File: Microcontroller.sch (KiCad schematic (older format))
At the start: 19 parts, among them P2 UART, P3 USB_B, P5 JTAG, U5 ATMEGA32U4RC-A, Y1 16MHz

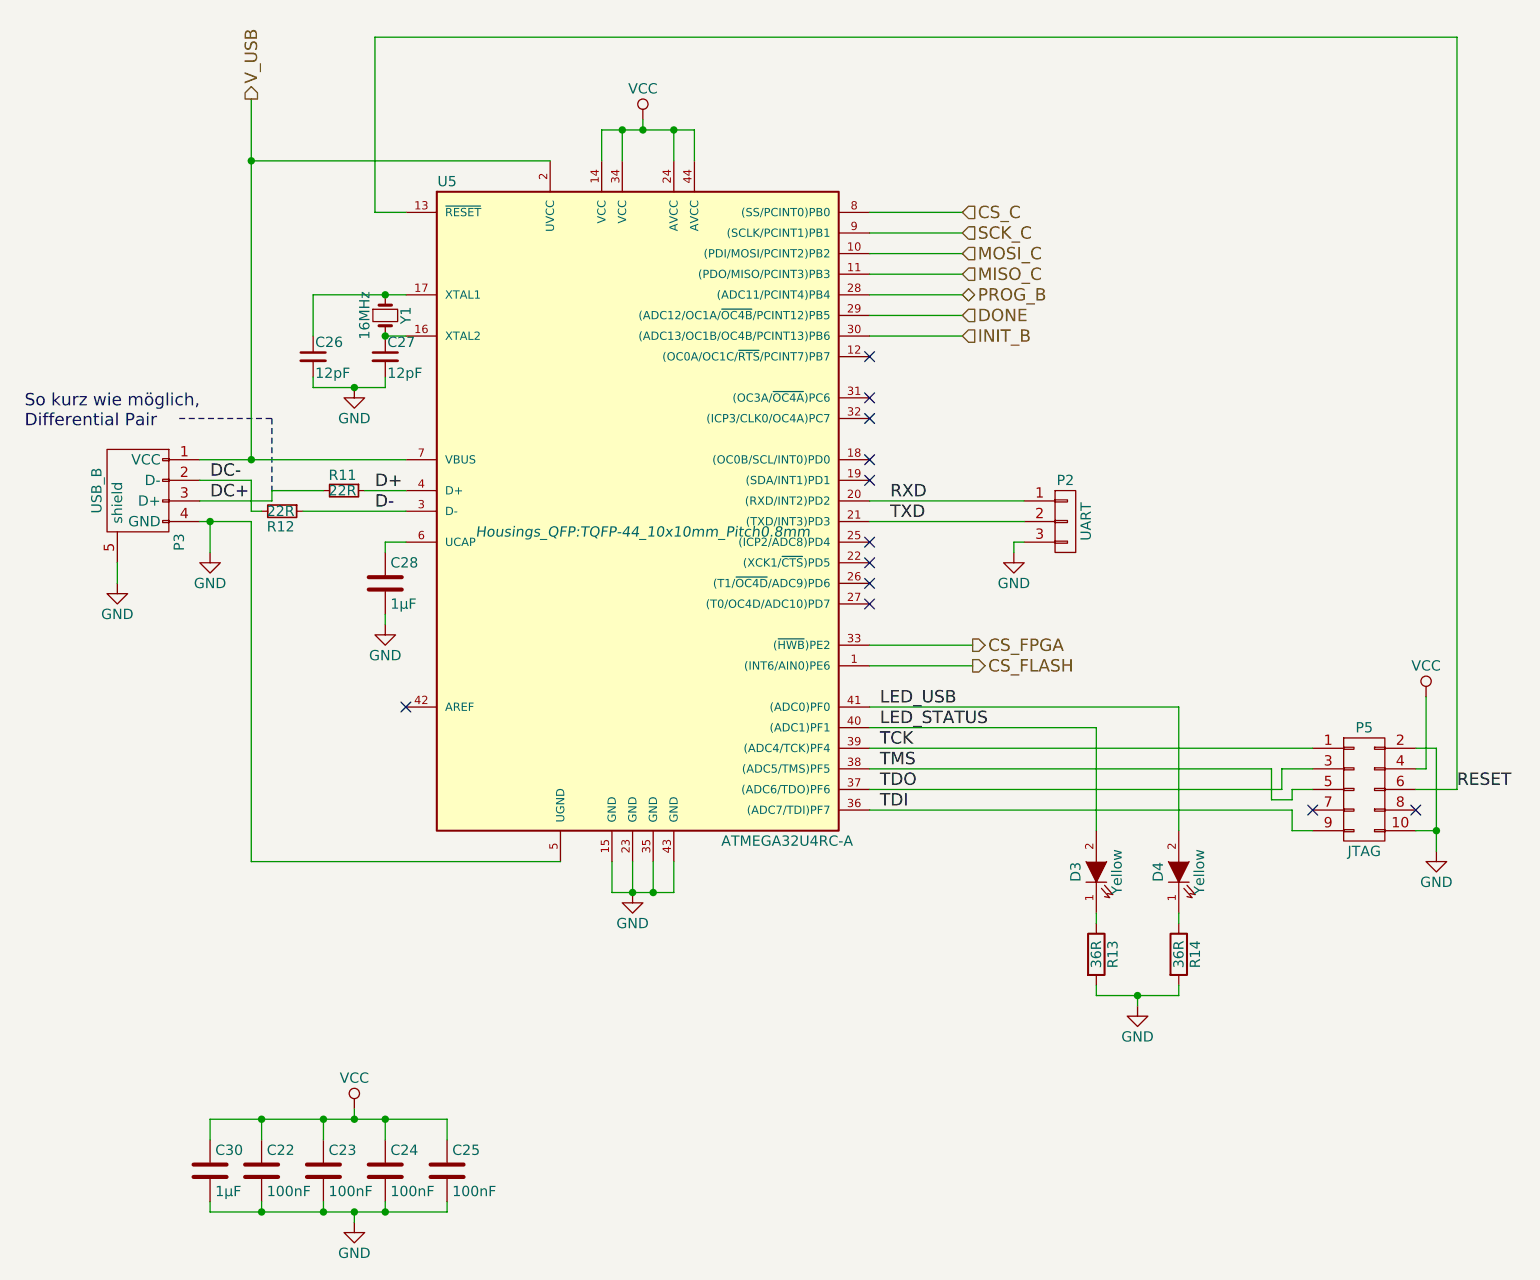
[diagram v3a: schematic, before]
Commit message: Added Resistor in Reset Line
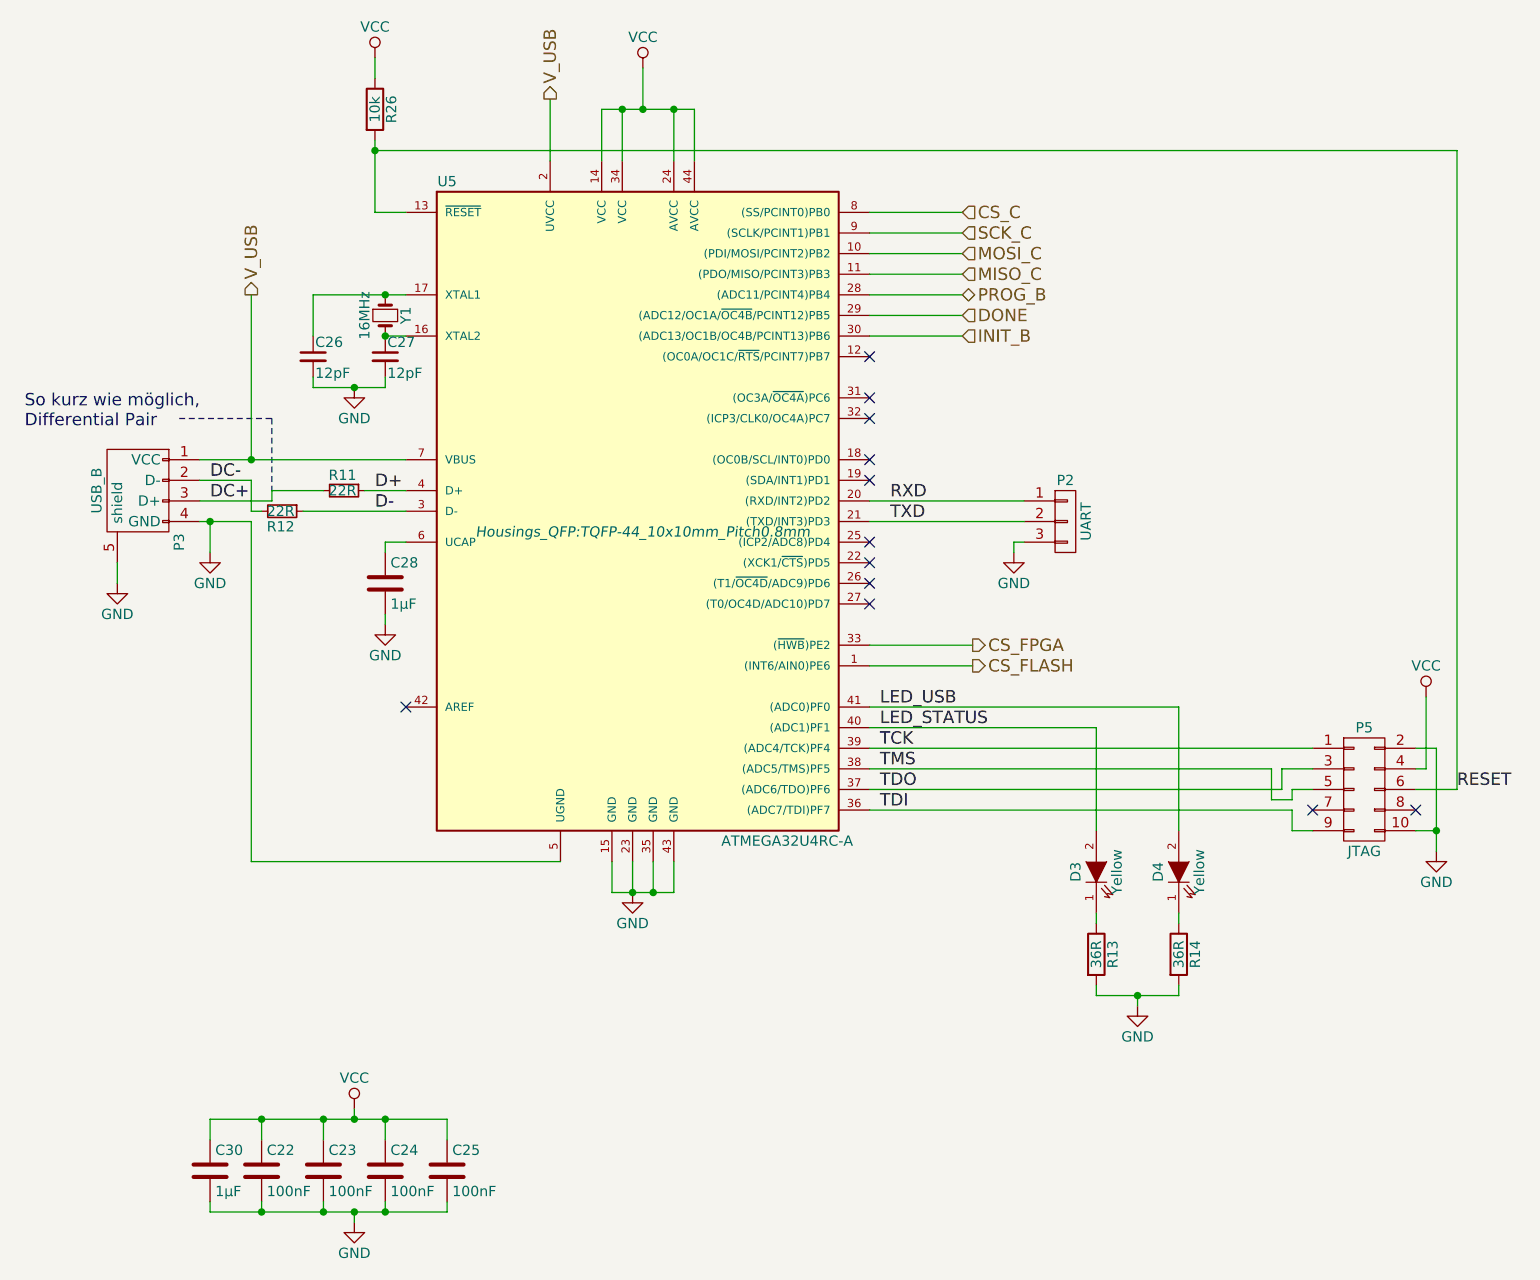
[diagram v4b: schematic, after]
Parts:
- added R26: 10k, Resistors_SMD:R_0805_HandSoldering, symbol R
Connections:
- net RESET: now also R26.2
- net VCC: now also R26.1
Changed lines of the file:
@@
 CS_C
 $Comp
-L GND #PWR024
+L GND #PWR33
 U 1 1 577EB04B
 P 4150 5550
-F 0 "#PWR024" H 4150 5300 50  0001 C CNN
+F 0 "#PWR33" H 4150 5300 50  0001 C CNN
 F 1 "GND" H 4150 5400 50  0000 C CNN
 F 2 "" H 4150 5550 50  0000 C CNN
@@
 $EndComp
 $Comp
-L GND #PWR025
+L GND #PWR27
 U 1 1 577EB215
 P 2100 3900
-F 0 "#PWR025" H 2100 3650 50  0001 C CNN
+F 0 "#PWR27" H 2100 3650 50  0001 C CNN
 F 1 "GND" H 2100 3750 50  0000 C CNN
 F 2 "" H 2100 3900 50  0000 C CNN
@@
 $EndComp
 $Comp
-L GND #PWR026
+L GND #PWR29
 U 1 1 577EB26B
 P 1650 4050
-F 0 "#PWR026" H 1650 3800 50  0001 C CNN
+F 0 "#PWR29" H 1650 3800 50  0001 C CNN
 F 1 "GND" H 1650 3900 50  0000 C CNN
 F 2 "" H 1650 4050 50  0000 C CNN
@@
 $EndComp
 $Comp
-L GND #PWR027
+L GND #PWR26
 U 1 1 5780F9B3
 P 2800 3100
-F 0 "#PWR027" H 2800 2850 50  0001 C CNN
+F 0 "#PWR26" H 2800 2850 50  0001 C CNN
 F 1 "GND" H 2800 2950 50  0000 C CNN
 F 2 "" H 2800 3100 50  0000 C CNN
@@
 $EndComp
 $Comp
-L GND #PWR028
+L GND #PWR30
 U 1 1 5780FD97
 P 2950 4250
-F 0 "#PWR028" H 2950 4000 50  0001 C CNN
+F 0 "#PWR30" H 2950 4000 50  0001 C CNN
 F 1 "GND" H 2950 4100 50  0000 C CNN
 F 2 "" H 2950 4250 50  0000 C CNN
@@
 	0    1    1    0
 $EndComp
-Text HLabel 2300 1700 1    60   Output ~ 0
+Text HLabel 2300 2650 1    60   Output ~ 0
 V_USB
 Text Notes 1200 3300 0    60   ~ 0
@@
 $EndComp
 $Comp
-L GND #PWR029
+L GND #PWR32
 U 1 1 57812B8C
 P 8050 5350
-F 0 "#PWR029" H 8050 5100 50  0001 C CNN
+F 0 "#PWR32" H 8050 5100 50  0001 C CNN
 F 1 "GND" H 8050 5200 50  0000 C CNN
 F 2 "" H 8050 5350 50  0000 C CNN
@@
 $EndComp
 $Comp
-L GND #PWR030
+L GND #PWR36
 U 1 1 57817BBC
 P 2800 7150
-F 0 "#PWR030" H 2800 6900 50  0001 C CNN
+F 0 "#PWR36" H 2800 6900 50  0001 C CNN
 F 1 "GND" H 2800 7000 50  0000 C CNN
 F 2 "" H 2800 7150 50  0000 C CNN
@@
 	2050 3450 3050 3450
 Wire Wire Line
-	2300 1700 2300 3450
-Wire Wire Line
-	2300 2000 3750 2000
+	2300 2650 2300 3450
 Connection ~ 2300 3450
 Wire Wire Line
@@
 Wire Wire Line
 	2850 3600 3050 3600
-Connection ~ 2300 2000
-Wire Wire Line
-	4200 1850 4200 1800
-Wire Wire Line
-	4000 1850 4450 1850
-Wire Wire Line
-	4000 1850 4000 2000
-Wire Wire Line
-	4450 1850 4450 2000
-Connection ~ 4200 1850
-Wire Wire Line
-	4100 2000 4100 1850
-Connection ~ 4100 1850
-Wire Wire Line
-	4350 2000 4350 1850
-Connection ~ 4350 1850
+Wire Wire Line
+	4200 1750 4200 1550
+Wire Wire Line
+	4000 1750 4450 1750
+Wire Wire Line
+	4000 1750 4000 2000
+Wire Wire Line
+	4450 1750 4450 2000
+Connection ~ 4200 1750
+Wire Wire Line
+	4100 2000 4100 1750
+Connection ~ 4100 1750
+Wire Wire Line
+	4350 2000 4350 1750
+Connection ~ 4350 1750
 Wire Notes Line
 	1950 3250 2400 3250
 Wire Notes Line
 	2400 3250 2400 3600
-Wire Wire Line
-	2900 1400 2900 2250
-Wire Wire Line
-	2900 2250 3050 2250
 Wire Wire Line
 	5300 4850 7450 4850
@@
 $EndComp
 $Comp
-L GND #PWR031
+L GND #PWR34
 U 1 1 5781915B
 P 6600 6100
-F 0 "#PWR031" H 6600 5850 50  0001 C CNN
+F 0 "#PWR34" H 6600 5850 50  0001 C CNN
 F 1 "GND" H 6600 5950 50  0000 C CNN
 F 2 "" H 6600 6100 50  0000 C CNN
@@
 RESET
 Wire Wire Line
-	2900 1400 8150 1400
-Wire Wire Line
-	8150 1400 8150 5050
+	8150 1950 8150 5050
 NoConn ~ 5300 2950
 $Comp
-L VCC #PWR032
+L VCC #PWR25
 U 1 1 57871A81
-P 4200 1800
-F 0 "#PWR032" H 4200 1650 50  0001 C CNN
-F 1 "VCC" H 4200 1950 50  0000 C CNN
-F 2 "" H 4200 1800 50  0000 C CNN
-F 3 "" H 4200 1800 50  0000 C CNN
-	1    4200 1800
-	1    0    0    -1
-$EndComp
-$Comp
-L VCC #PWR033
+P 4200 1550
+F 0 "#PWR25" H 4200 1400 50  0001 C CNN
+F 1 "VCC" H 4200 1700 50  0000 C CNN
+F 2 "" H 4200 1550 50  0000 C CNN
+F 3 "" H 4200 1550 50  0000 C CNN
+	1    4200 1550
+	1    0    0    -1
+$EndComp
+$Comp
+L VCC #PWR31
 U 1 1 57871EAB
 P 8000 4600
-F 0 "#PWR033" H 8000 4450 50  0001 C CNN
+F 0 "#PWR31" H 8000 4450 50  0001 C CNN
 F 1 "VCC" H 8000 4750 50  0000 C CNN
 F 2 "" H 8000 4600 50  0000 C CNN
@@
 $EndComp
 $Comp
-L VCC #PWR034
+L VCC #PWR35
 U 1 1 578720B7
 P 2800 6600
-F 0 "#PWR034" H 2800 6450 50  0001 C CNN
+F 0 "#PWR35" H 2800 6450 50  0001 C CNN
 F 1 "VCC" H 2800 6750 50  0000 C CNN
 F 2 "" H 2800 6600 50  0000 C CNN
@@
 	5300 3650 6050 3650
 $Comp
-L GND #PWR035
+L GND #PWR28
 U 1 1 5897F234
 P 6000 3900
-F 0 "#PWR035" H 6000 3650 50  0001 C CNN
+F 0 "#PWR28" H 6000 3650 50  0001 C CNN
 F 1 "GND" H 6000 3750 50  0000 C CNN
 F 2 "" H 6000 3900 50  0000 C CNN
@@
 Wire Wire Line
 	5300 2850 5750 2850
+$Comp
+L R R26
+U 1 1 58BD31F6
+P 2900 1750
+F 0 "R26" V 2980 1750 50  0000 C CNN
+F 1 "10k" V 2900 1750 50  0000 C CNN
+F 2 "Resistors_SMD:R_0805_HandSoldering" V 2830 1750 50  0001 C CNN
+F 3 "" H 2900 1750 50  0000 C CNN
+	1    2900 1750
+	1    0    0    -1
+$EndComp
+$Comp
+L VCC #PWR24
+U 1 1 58BD38E2
+P 2900 1500
+F 0 "#PWR24" H 2900 1350 50  0001 C CNN
+F 1 "VCC" H 2900 1650 50  0000 C CNN
+F 2 "" H 2900 1500 50  0000 C CNN
+F 3 "" H 2900 1500 50  0000 C CNN
+	1    2900 1500
+	1    0    0    -1
+$EndComp
+Text HLabel 3750 1700 1    60   Output ~ 0
+V_USB
+Wire Wire Line
+	3750 2000 3750 1700
+Wire Wire Line
+	2900 2250 3050 2250
+Wire Wire Line
+	2900 1900 2900 2250
+Wire Wire Line
+	2900 1500 2900 1600
+Wire Wire Line
+	2900 1950 8150 1950
+Connection ~ 2900 1950
 $EndSCHEMATC
